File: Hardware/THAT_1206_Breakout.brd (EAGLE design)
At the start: 100.3 x 20.3 mm, 42 parts, among them IC1 THAT1206, IC2 THAT1646, J1 INPUT, J2 OUTPUT, J3 CHASSIS, J6 CHASSIS

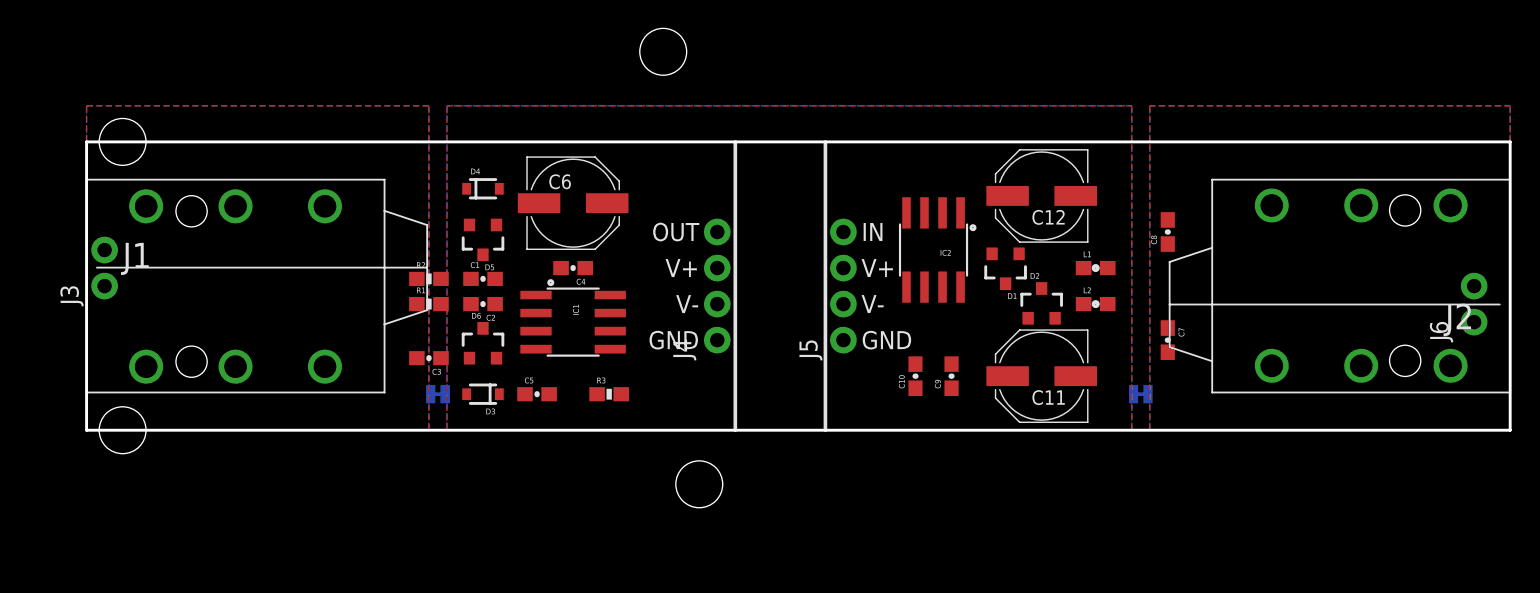
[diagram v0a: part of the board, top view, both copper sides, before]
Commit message: Broke into 2 separate board files.
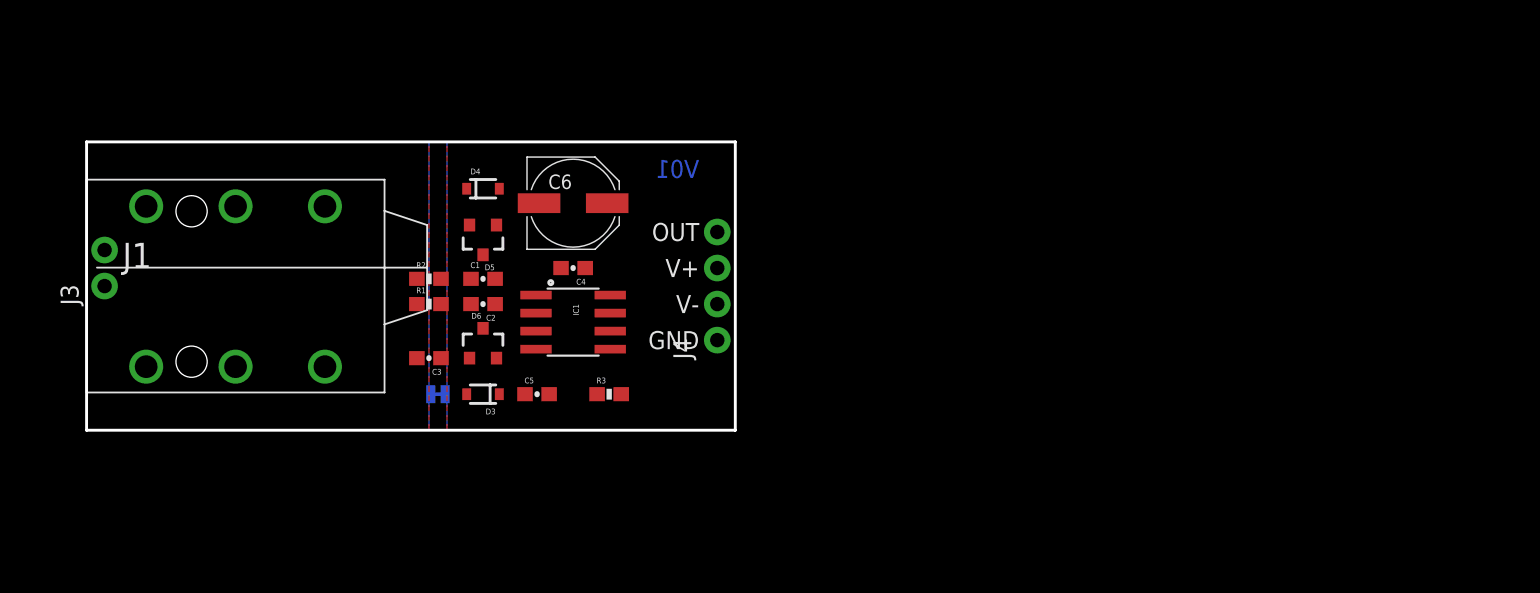
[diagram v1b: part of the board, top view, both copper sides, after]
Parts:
- removed C10, C9: 0.1uF, SparkFun-Capacitors:0603-CAP
- removed C11, C12: 10uf, that-ics:PANASONIC_D
- removed C7, C8: 100pF, SparkFun-Capacitors:0603-CAP
- removed D1, D2: (no value), SparkFun-DiscreteSemi:SOT23-3
- removed H1, H2, H3, H4: STAND-OFF, SparkFun-Electromechanical:STAND-OFF
- removed IC2: THAT1646, that-ics:SO08
- removed J2: OUTPUT, SparkFun-Connectors:AUDIO-JACK-.25-INCH-HORIZ-PTH
- removed J5: (no value), SparkFun-Connectors:1X04_NO_SILK_ALL_ROUND
- removed J6: CHASSIS, SparkFun-Connectors:1X02_NO_SILK
- removed JP2: JUMPER-PAD-2-NC_BY_TRACE, SparkFun-Passives:PAD-JUMPER-2-NC_BY_TRACE_YES_SILK
- removed L1, L2: 27uH, SparkFun-Passives:0603
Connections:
- removed net N$10: C11.-, D2.3, IC2.8, L2.1
- removed net N$11: C12.-, D1.3, IC2.1, L1.1
- removed net N$13: C12.+, IC2.2
- removed net N$14: C11.+, IC2.7
- removed net N$16: IC2.4, J5.4
- removed net N$8: C8.1, J2.TIP, L2.2
- removed net N$9: C7.1, J2.RING, L1.2
- net GND: no longer C10.1, C9.1, IC2.3, J5.1, JP2.2
- net GND-ISO: no longer C7.2, C8.2, J2.SLEEVE, J6.1, J6.2, JP2.1
- net VCC: no longer C9.2, D1.2, D2.2, IC2.6, J5.3
- net VNEG: no longer C10.2, D1.1, D2.1, IC2.5, J5.2
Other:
- board size 100.3 x 20.3 mm -> 45.7 x 20.3 mm
- board text added: "Byron Jacquot"
- board text added: "V01"
- board text removed: "IN"

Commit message: Routed PCB.
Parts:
- removed H5, H6, H7, H8: STAND-OFF, SparkFun-Electromechanical:STAND-OFF
- added FD1, FD2: FIDUCIALUFIDUCIAL, SparkFun-Aesthetics:MICRO-FIDUCIAL
- added LOGO1: SFE_LOGO_NAME.1_INCH, SparkFun-Aesthetics:SFE_LOGO_NAME_.1
- added LOGO2, LOGO5: OSHW-LOGOS, SparkFun-Aesthetics:OSHW-LOGO-S
- added LOGO4: SFE_LOGO_FLAME.2_INCH, SparkFun-Aesthetics:SFE_LOGO_FLAME_.2
- moved R3 12.0 mm to (26.9, 9.40), turned to 270 degrees
- moved C4 9.73 mm to (27.9, 18.8)
- moved C5 8.89 mm to (40.6, 2.54)
- moved C3 5.08 mm to (24.1, 10.2)
- moved R2 5.08 mm to (24.1, 15.7)
- moved R1 3.81 mm to (24.1, 5.08)
- moved D3 3.56 mm to (31.5, 2.54)
- moved C1 3.25 mm to (25.4, 12.7), turned to 270 degrees
- moved C2 2.84 mm to (25.4, 7.62), turned to 270 degrees
- moved D5 2.62 mm to (29.2, 11.2)
- moved D4 2.17 mm to (28.7, 15.0), turned to 90 degrees
- moved D6 1.38 mm to (29.2, 6.62), turned to 180 degrees
- moved J4 1.27 mm to (43.2, 6.35)
- moved C6 0.57 mm to (34.5, 16.5), turned to 180 degrees
- moved IC1 0.51 mm to (34.8, 7.62), turned to 0 degrees
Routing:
- net VCC: track 0.00 -> 23.5 mm, vias 0 -> 3
- net N$6: track 0.00 -> 20.2 mm, vias 0 -> 2
- net N$2: track 0.00 -> 19.1 mm, vias 0 -> 3
- net VNEG: track 0.00 -> 18.7 mm
- net N$4: track 0.00 -> 17.6 mm, vias 0 -> 2
- net N$1: track 0.00 -> 17.4 mm
- net RCV: track 0.00 -> 10.4 mm, vias 0 -> 1
- net N$12: track 0.00 -> 9.71 mm
- net N$3: track 0.00 -> 6.73 mm
- net N$7: track 0.00 -> 6.58 mm
- net N$15: track 0.00 -> 6.40 mm
- net N$5: track 0.00 -> 5.71 mm
- net GND-ISO: track 0.00 -> 1.40 mm
- net GND: track 0.00 -> 1.40 mm, vias 0 -> 3
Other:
- board size 45.7 x 20.3 mm -> 44.5 x 20.3 mm
- board text added: "Chassis"
- board text added: "Cut jumper to isolate chassis and circuit grounds"
- board text added: "THAT 1206 Breakout"
- board text added: "THAT 1206 InGenius Line Receiver Breakout"

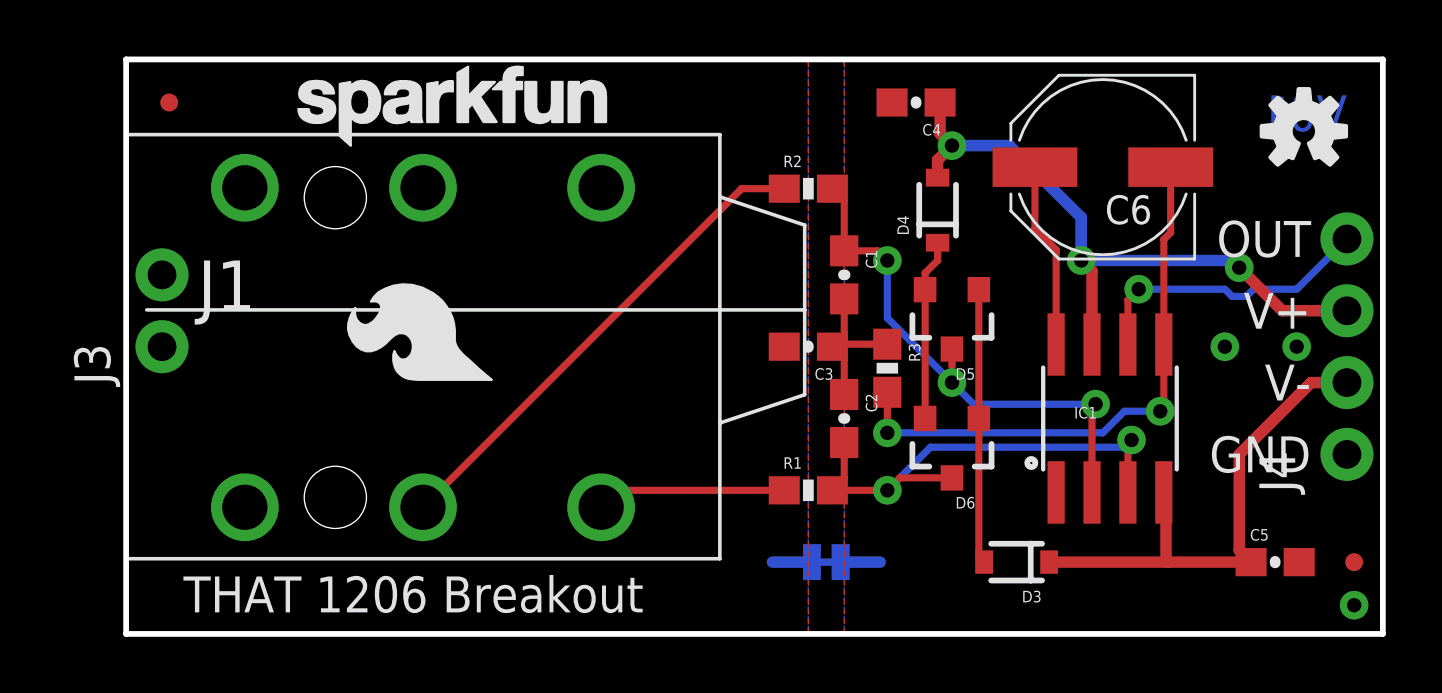
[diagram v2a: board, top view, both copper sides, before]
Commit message: Updates after routing.
Added ground stitches & dimensions.
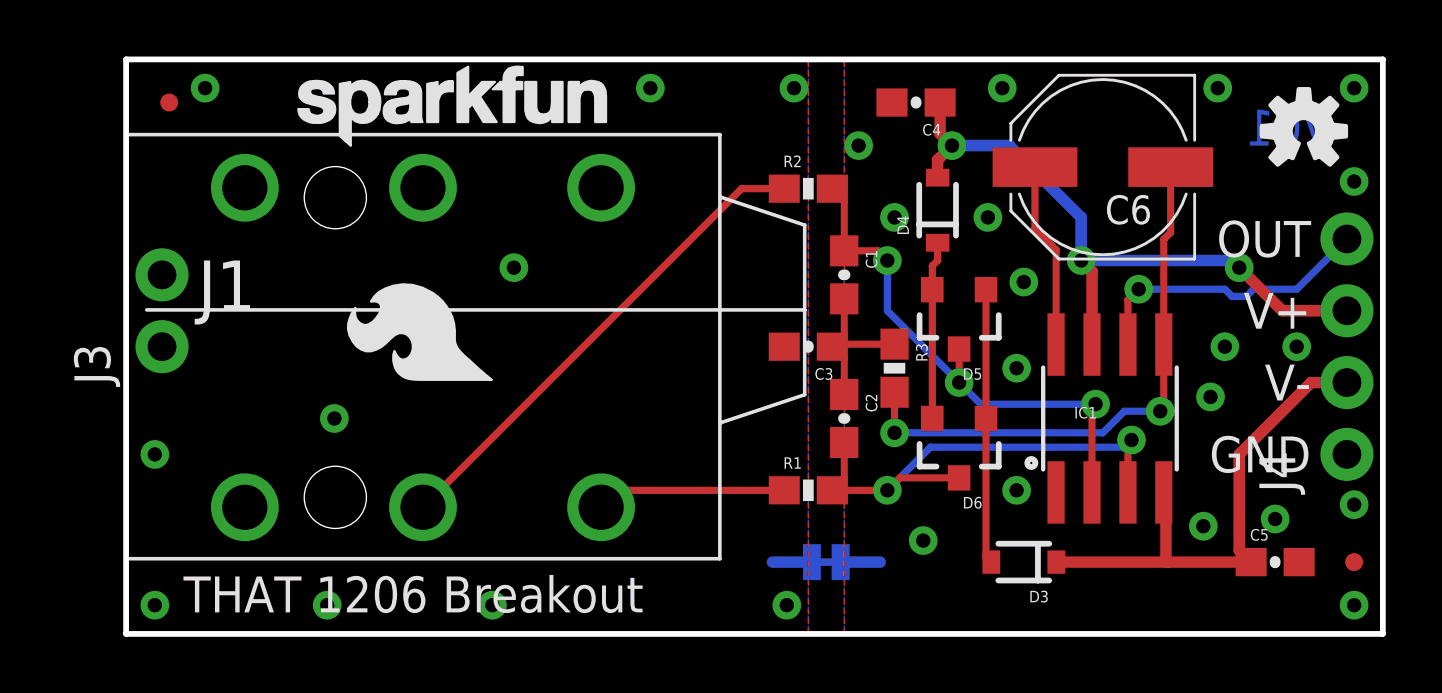
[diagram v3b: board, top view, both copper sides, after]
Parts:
- moved D3 0.25 mm to (31.8, 2.54)
- moved R3 0.25 mm to (27.2, 9.40)
- moved D5 0.25 mm to (29.5, 11.2)
- moved D6 0.25 mm to (29.5, 6.62)
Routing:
- net GND-ISO: vias 0 -> 10
- net GND: vias 3 -> 18
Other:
- board text added: "Drill 3/8" hole to accomodate TRS jack"

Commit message: After proto review.
Many fit & finish changes.
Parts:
- removed D5: (no value), SparkFun-DiscreteSemi:SOT23-3
- added D1: 12V, that-ics:SOD-323
- added FD3, FD4: FIDUCIALUFIDUCIAL, SparkFun-Aesthetics:MICRO-FIDUCIAL
- added J2: INPUT, SparkFun-Connectors:AUDIO-JACK-.25-INCH-HORIZ-PTH
- added J5: TN, SparkFun-Connectors:1X01_NO_SILK
- added J6: SN, SparkFun-Connectors:1X01_NO_SILK
- added LOGO3: OSHW-LOGOS, SparkFun-Aesthetics:OSHW-LOGO-S
- C4: value 0.1uF -> 220uf; device SparkFun-Capacitors:0603-CAP -> that-ics:PANASONIC_D
- C6: value 220uf -> 0.1uF; device that-ics:PANASONIC_D -> SparkFun-Capacitors:0603-CAP
- D2: value (none) -> BAV99
- D3: value 12V -> BAV99; device that-ics:SOD-323 -> SparkFun-DiscreteSemi:SOT23-3
- J1: value INPUT -> CHASSIS; device SparkFun-Connectors:AUDIO-JACK-.25-INCH-HORIZ-PTH -> SparkFun-Connectors:1X02_NO_SILK
- J3: value CHASSIS -> (none); device SparkFun-Connectors:1X02_NO_SILK -> SparkFun-Connectors:1X04_NO_SILK_ALL_ROUND
- J4: value (none) -> RN; device SparkFun-Connectors:1X04_NO_SILK_ALL_ROUND -> SparkFun-Connectors:1X01_NO_SILK
- LOGO1: value SFE_LOGO_NAME.1_INCH -> SFE_LOGO_FLAME.2_INCH; device SparkFun-Aesthetics:SFE_LOGO_NAME_.1 -> SparkFun-Aesthetics:SFE_LOGO_FLAME_.2
- LOGO4: value SFE_LOGO_FLAME.2_INCH -> SFE_LOGO_NAME.1_INCH; device SparkFun-Aesthetics:SFE_LOGO_FLAME_.2 -> SparkFun-Aesthetics:SFE_LOGO_NAME_.1
- LOGO5: value OSHW-LOGOS -> SFE_LOGO_FLAME.2_INCH; device SparkFun-Aesthetics:OSHW-LOGO-S -> SparkFun-Aesthetics:SFE_LOGO_FLAME_.2
- moved J3 42.1 mm to (43.2, 6.35)
- moved LOGO5 29.4 mm to (12.7, 12.7), flipped to the bottom, turned to 270 degrees
- moved J4 27.3 mm to (19.1, 19.1), turned to 0 degrees
- moved C5 20.3 mm to (28.2, 18.5), turned to 180 degrees
- moved C6 15.2 mm to (40.6, 2.54), turned to 0 degrees
- moved R2 13.5 mm to (24.9, 2.29)
- moved R1 11.7 mm to (24.9, 16.8)
- moved LOGO4 11.2 mm to (5.21, 16.5), turned to 0 degrees
- moved LOGO1 10.6 mm to (12.7, 8.89), turned to 90 degrees
- moved D3 8.93 mm to (29.5, 11.2)
- moved C4 6.99 mm to (34.5, 16.5)
- moved C2 3.78 mm to (26.7, 4.06), turned to 0 degrees
- moved FD1 3.34 mm to (4.83, 19.3)
- moved C3 3.14 mm to (24.9, 7.11)
- moved J1 1.80 mm to (1.27, 10.2), turned to 90 degrees
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- renumbered D6 to D2
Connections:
- new net N$10: J2.RING-NORM, J4.1
- new net N$8: J2.SLEEVE-NORM, J6.1
- new net N$9: J2.TIP-NORM, J5.1
- net GND: now also C6.2, J3.1; no longer C4.2, J4.1
- net GND-ISO: now also J1.1, J1.2, J2.SLEEVE; no longer J1.SLEEVE, J3.1, J3.2
- net N$1: now also J2.RING, R1.1; no longer J1.RING, R2.1
- net N$12: now also D1.A, D3.1; no longer D3.A, D5.1
- net N$15: now also D3.2; no longer D5.2
- net N$2: now also D3.3, R1.2; no longer D5.3, R2.2
- net N$3: now also J2.TIP, R2.1; no longer J1.TIP, R1.1
- net N$4: now also R2.2; no longer R1.2
- net N$6: now also C4.-; no longer C6.-
- net N$7: now also C4.+; no longer C6.+
- net RCV: now also J3.4; no longer J4.4
- net VCC: now also C5.1, J3.3; no longer C4.1, J4.3
- net VNEG: now also C6.1, D1.C, J3.2; no longer C5.1, D3.C, J4.2
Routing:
- net N$10: track 0.00 -> 9.90 mm
- net N$9: track 0.00 -> 6.14 mm
- net N$8: track 0.00 -> 4.48 mm
- net N$5: track 5.96 -> 8.92 mm
- net N$2: track 18.9 -> 20.6 mm
- net N$3: track 6.73 -> 8.15 mm
- net N$1: track 17.4 -> 18.6 mm
- net N$4: track 17.8 -> 16.7 mm
- net N$6: track 19.9 -> 20.7 mm
- net GND-ISO: vias 10 -> 15
- net GND: vias 18 -> 19
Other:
- board text added: "All dimensions in inches."
- board text added: "Drill 0.44" (11mm) hole to accomodate TRS jack"
- board text added: "RN"
- board text added: "SN"
- board text added: "TN"
- board text removed: "Drill 3/8" hole to accomodate TRS jack"

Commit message: Fixing the nonpolar caps
To have non-polarized schem symbols, and adding PROD_IDs.
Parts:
- added LOGO6: SFE_LOGO_NAME.1_INCH, SparkFun-Aesthetics:SFE_LOGO_NAME_.1
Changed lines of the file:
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@@
 <element name="J5" library="SparkFun-Connectors" package="1X01_NO_SILK" value="TN" x="21.59" y="19.05"/>
 <element name="J6" library="SparkFun-Connectors" package="1X01_NO_SILK" value="SN" x="1.27" y="19.05"/>
+<element name="LOGO6" library="SparkFun-Aesthetics" package="SFE_LOGO_NAME_.1" value="SFE_LOGO_NAME.1_INCH" x="17.145" y="16.51" rot="MR0"/>
 </elements>
 <signals>

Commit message: Ran engineering checklist, a few small changes.
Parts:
- J1: value CHASSIS -> INPUT; device SparkFun-Connectors:1X02_NO_SILK -> SparkFun-Connectors:AUDIO-JACK-.25-INCH-HORIZ-PTH
- J2: value INPUT -> CHASSIS; device SparkFun-Connectors:AUDIO-JACK-.25-INCH-HORIZ-PTH -> SparkFun-Connectors:1X02_NO_SILK
- J3: value (none) -> RN; device SparkFun-Connectors:1X04_NO_SILK_ALL_ROUND -> SparkFun-Connectors:1X01_NO_SILK
- J4: value RN -> TN
- J5: value TN -> SN
- J6: value SN -> 1x4; device SparkFun-Connectors:1X01_NO_SILK -> SparkFun-Connectors:1X04_NO_SILK_ALL_ROUND
- LOGO2: value OSHW-LOGOS -> SFE_LOGO_FLAME.2_INCH; device SparkFun-Aesthetics:OSHW-LOGO-S -> SparkFun-Aesthetics:SFE_LOGO_FLAME_.2
- LOGO4: value SFE_LOGO_NAME.1_INCH -> OSHW-LOGOS; device SparkFun-Aesthetics:SFE_LOGO_NAME_.1 -> SparkFun-Aesthetics:OSHW-LOGO-S
- LOGO5: value SFE_LOGO_FLAME.2_INCH -> SFE_LOGO_NAME.1_INCH; device SparkFun-Aesthetics:SFE_LOGO_FLAME_.2 -> SparkFun-Aesthetics:SFE_LOGO_NAME_.1
- moved J6 43.8 mm to (43.2, 6.35), turned to 90 degrees
- moved FD1 42.1 mm to (43.4, 2.54), flipped to the bottom
- moved FD2 42.1 mm to (4.83, 19.3), flipped to the bottom, turned to 90 degrees
- moved FD3 42.1 mm to (4.83, 19.3), flipped to the top
- moved FD4 42.1 mm to (43.4, 2.54), flipped to the top, turned to 0 degrees
- moved LOGO4 35.9 mm to (41.1, 17.3)
- moved J3 27.3 mm to (19.1, 19.1), turned to 0 degrees
- moved LOGO2 24.6 mm to (12.7, 12.7), turned to 270 degrees
- moved J5 20.3 mm to (1.27, 19.1)
- moved LOGO5 8.41 mm to (5.21, 16.5), flipped to the top, turned to 0 degrees
- moved LOGO3 4.32 mm to (36.8, 17.3), flipped to the bottom
- moved J4 2.54 mm to (21.6, 19.1)
- moved J1 1.80 mm to (0.00, 11.4), turned to 0 degrees
- moved J2 1.80 mm to (1.27, 10.2), turned to 90 degrees
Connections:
- net GND: now also J6.1; no longer J3.1
- net GND-ISO: now also J1.SLEEVE, J2.1, J2.2; no longer J1.1, J1.2, J2.SLEEVE
- net N$1: now also J1.RING; no longer J2.RING
- net N$10: now also J1.RING-NORM, J3.1; no longer J2.RING-NORM, J4.1
- net N$3: now also J1.TIP; no longer J2.TIP
- net N$8: now also J1.SLEEVE-NORM, J5.1; no longer J2.SLEEVE-NORM, J6.1
- net N$9: now also J1.TIP-NORM, J4.1; no longer J2.TIP-NORM, J5.1
- net RCV: now also J6.4; no longer J3.4
- net VCC: now also J6.3; no longer J3.3
- net VNEG: now also J6.2; no longer J3.2
